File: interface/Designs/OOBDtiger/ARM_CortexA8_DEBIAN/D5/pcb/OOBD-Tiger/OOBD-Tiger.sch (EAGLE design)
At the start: 128 parts, among them IC1 ADM3053M, IC2 ADM3053M, IC4 DS3231, U1 SY6280, U10 MP1482DS, U2 SN65HVD230(SO8), U3 SY6280, U4 TLV70215, U6 SN65HVD230(SO8)

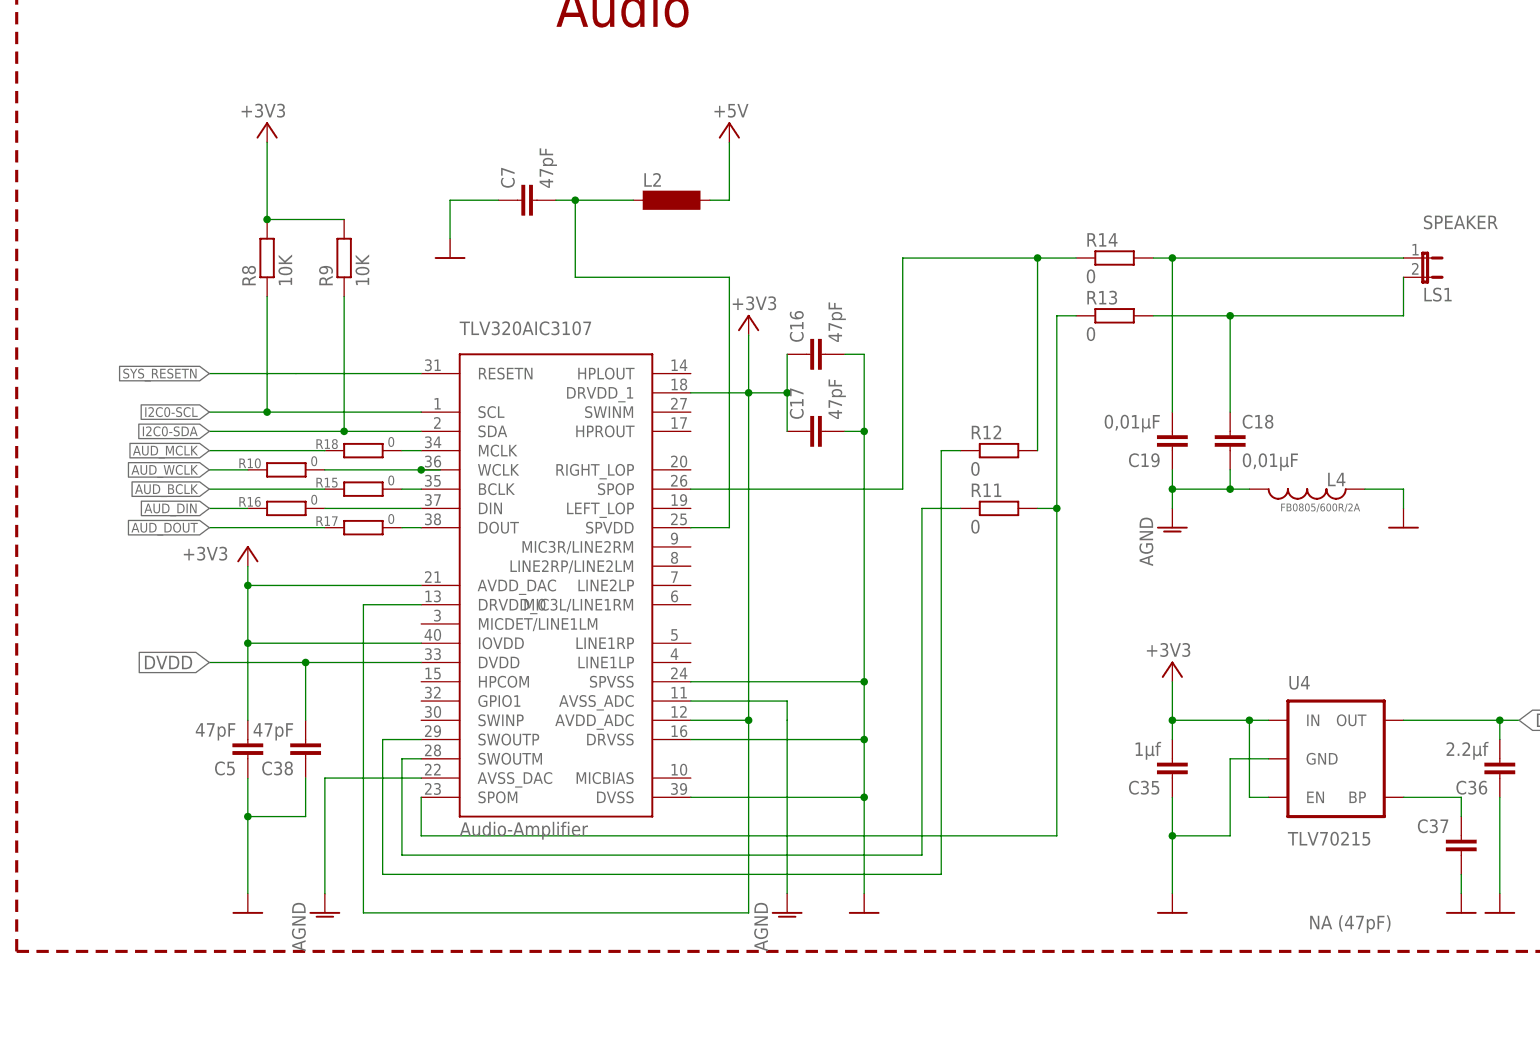
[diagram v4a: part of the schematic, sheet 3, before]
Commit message: Modification according 107EVM
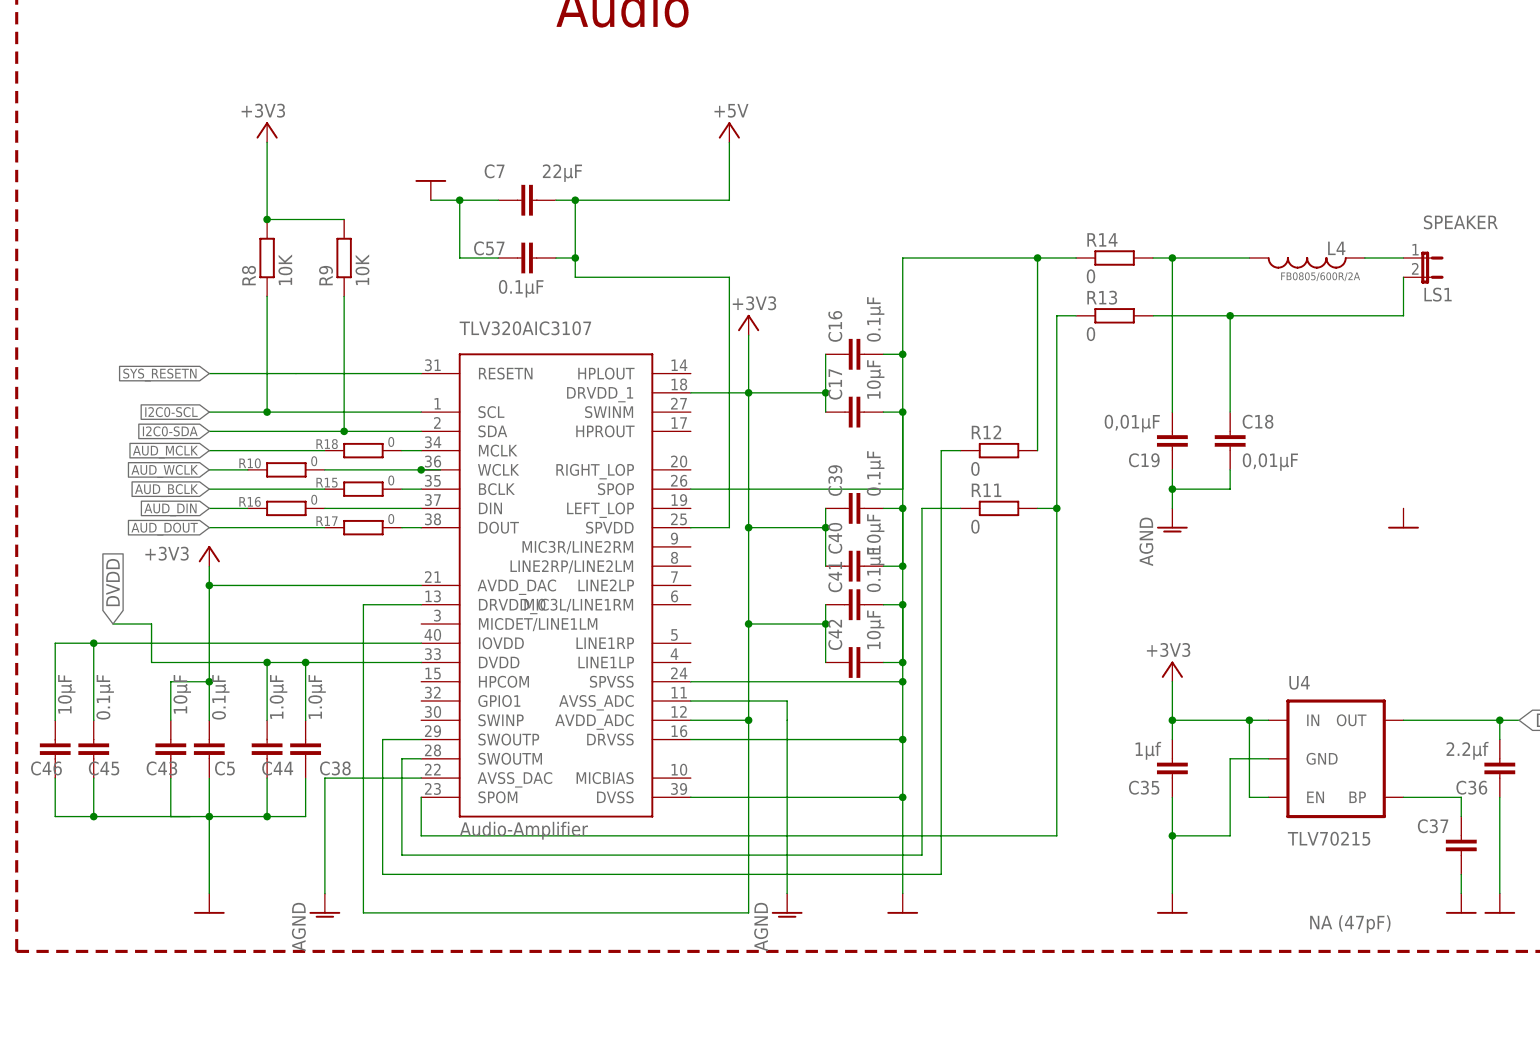
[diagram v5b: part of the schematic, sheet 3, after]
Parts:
- removed L2: (no value), inductor-neosid:SM-L15B
- added C39, C41, C45, C57: 0.1µF, SparkFun-Passives:CAP0603-CAP
- added C40, C42, C43, C46: 10µF, SparkFun-Passives:CAP0603-CAP
- added C44: 1.0µF, SparkFun-Passives:CAP0603-CAP
- C16, C5: value 47pF -> 0.1µF
- C17: value 47pF -> 10µF
- C38: value 47pF -> 1.0µF
- C7: value 47pF -> 22µF
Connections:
- removed net N$17: C7.2, L2.1, TLV320AIC3107.SPVDD
- new net GND1: C45.1, C46.1
- new net N$16: L4.1, SPEAKER.1
- net +3V3: now also C39.1, C40.1, C41.1, C42.1, C43.2; no longer TLV320AIC3107.IOVDD
- net +5V: now also C57.2, C7.2, TLV320AIC3107.SPVDD; no longer L2.2
- net AGND: no longer L4.2
- net DVDD: now also C44.2
- net GND: now also C39.2, C40.2, C41.2, C42.2, C43.1, C44.1, C57.1, R12.2, R14.1, TLV320AIC3107.SPOP; no longer L4.1
- net N$14: now also L4.2; no longer SPEAKER.1
- net N$21: now also C45.2, C46.2, TLV320AIC3107.IOVDD; no longer R12.2, R14.1, TLV320AIC3107.SPOP
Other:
- moved on the sheet: C16, C17, C5, L4
